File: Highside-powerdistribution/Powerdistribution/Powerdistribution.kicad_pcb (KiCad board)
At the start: 2 copper layers, 90 x 100 mm, 12 parts, among them J1 Screw_Terminal_01x02, J2 Screw_Terminal_01x02, J3 Screw_Terminal_01x02, J4 Screw_Terminal_01x02, J5 Screw_Terminal_01x02, J6 Screw_Terminal_01x02, J7 Screw_Terminal_01x02, J8 Screw_Terminal_01x02, J9 Screw_Terminal_01x02

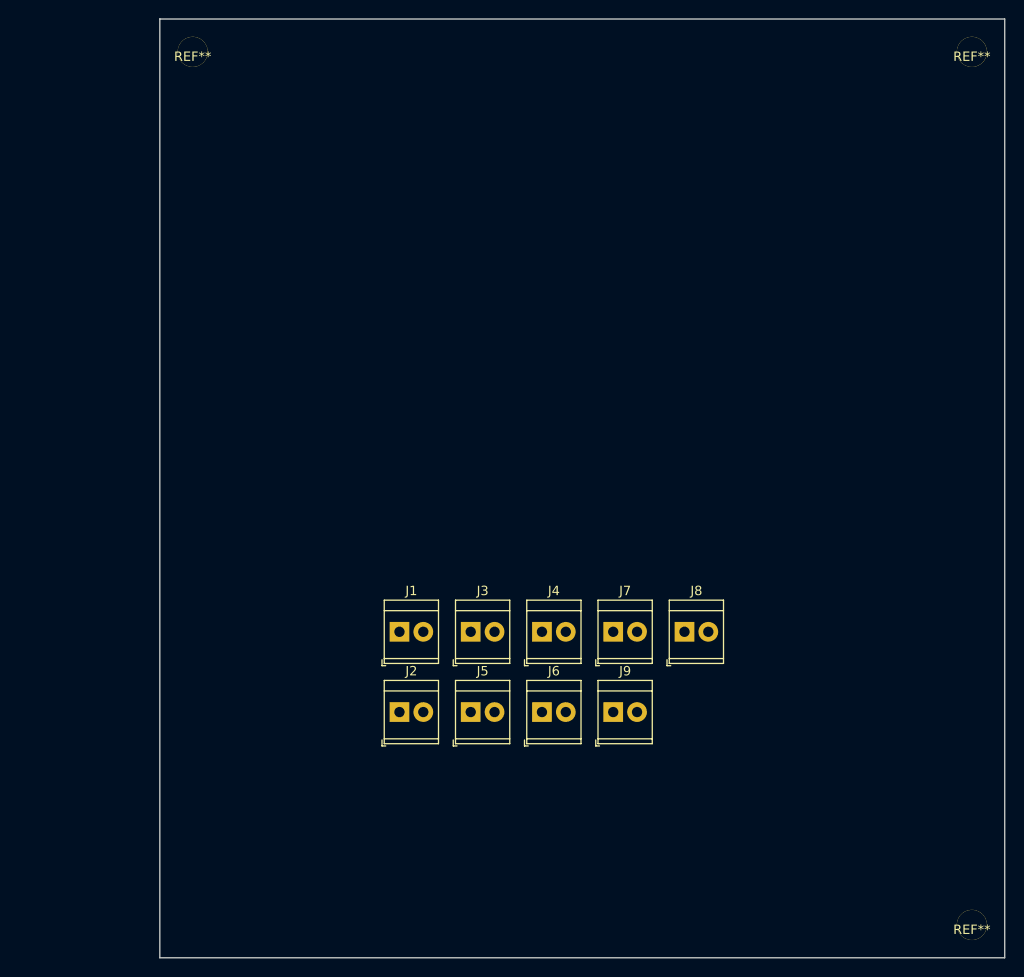
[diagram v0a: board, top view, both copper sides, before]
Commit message: Moved filled zone to remove shortcurcit
12V and the mosfets had filled zone together
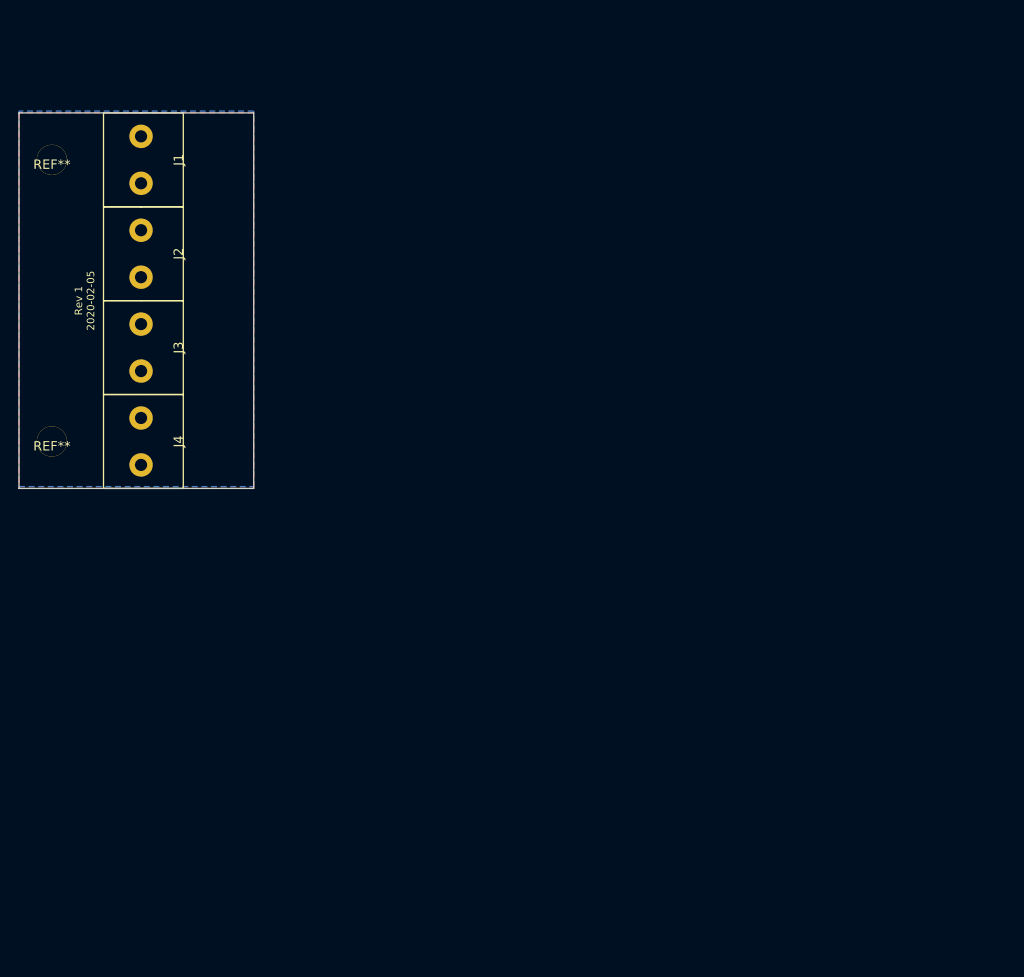
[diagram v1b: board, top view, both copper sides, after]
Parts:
- removed J5, J6, J7, J8, J9: Screw_Terminal_01x02, TerminalBlock_TE-Connectivity:TerminalBlock_TE_282834-2_1x02_P2.54mm_Horizontal
- removed the REF** at (201.5, 136.5)
- removed the REF** at (201.5, 43.5)
- removed the REF** at (118.5, 43.5)
- added REF**: Mountinghole, Highside-powerdistribution:Mountinghole, F.Cu at (103.5, 55.0)
- added REF**: Mountinghole, Highside-powerdistribution:Mountinghole, F.Cu at (103.5, 85.0)
- J1, J2, J3, J4: footprint TerminalBlock_TE-Connectivity:TerminalBlock_TE_282834-2_1x02_P2.54mm_Horizontal -> Highside-powerdistribution:Phoenix_TB_2-1935776
- moved J1 57.3 mm to (113.0, 55.0), turned to 90 degrees
- moved J2 56.0 mm to (113.0, 65.0), turned to 90 degrees
- moved J4 47.3 mm to (113.0, 85.0), turned to 90 degrees
- moved J3 46.4 mm to (113.0, 75.0), turned to 90 degrees
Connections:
- J1 pad 2: Net-(J1-Pad2) -> Net-(J1-Pad1)
- J2 pad 1: Net-(J2-Pad1) -> Net-(J1-Pad1)
- J2 pad 2: Net-(J2-Pad2) -> Net-(J1-Pad1)
- J3 pad 1: Net-(J3-Pad1) -> Net-(J1-Pad1)
- J3 pad 2: Net-(J3-Pad2) -> Net-(J1-Pad1)
- J4 pad 1: Net-(J4-Pad1) -> Net-(J1-Pad1)
- J4 pad 2: Net-(J4-Pad2) -> Net-(J1-Pad1)
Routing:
- added copper zone on B.Cu, net Net-(J1-Pad1)
- added copper zone on F.Cu, net Net-(J1-Pad1)
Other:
- board size 90 x 100 mm -> 25 x 40 mm
- board text added: "Rev 1 2020-02-05"
